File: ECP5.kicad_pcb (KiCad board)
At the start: 4 copper layers, 54.6 x 54.6 mm, 115 parts, among them J1 USB Type C, J2 EXT, Q1 MMST2222A, SW1 User, U1 LFE5U-85F-8BG381C, U2 IS25LP128F, U3 FT231XQ, U4 IS66WVE4M16EBLL-70BLI, U5 TLV62569DBVT, U6 TLV62569DBVT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

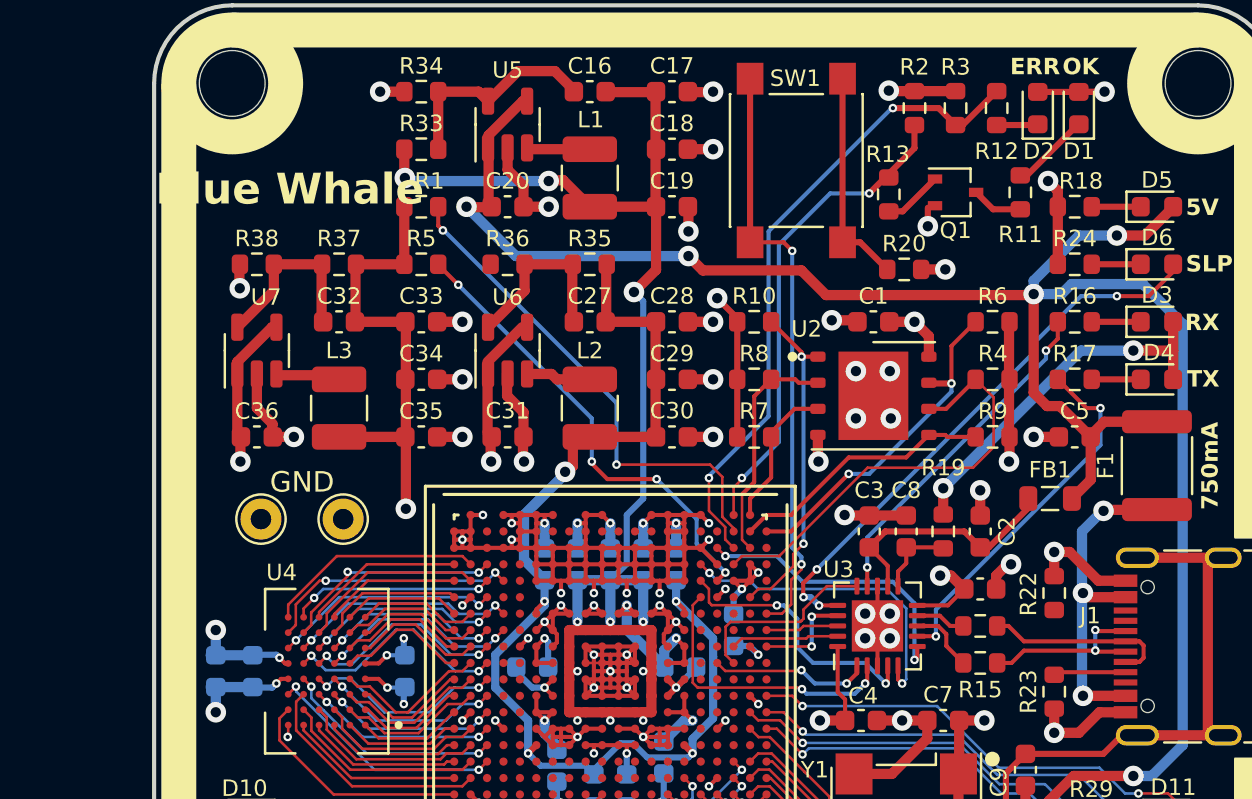
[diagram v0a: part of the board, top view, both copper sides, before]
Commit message: Switched to project library
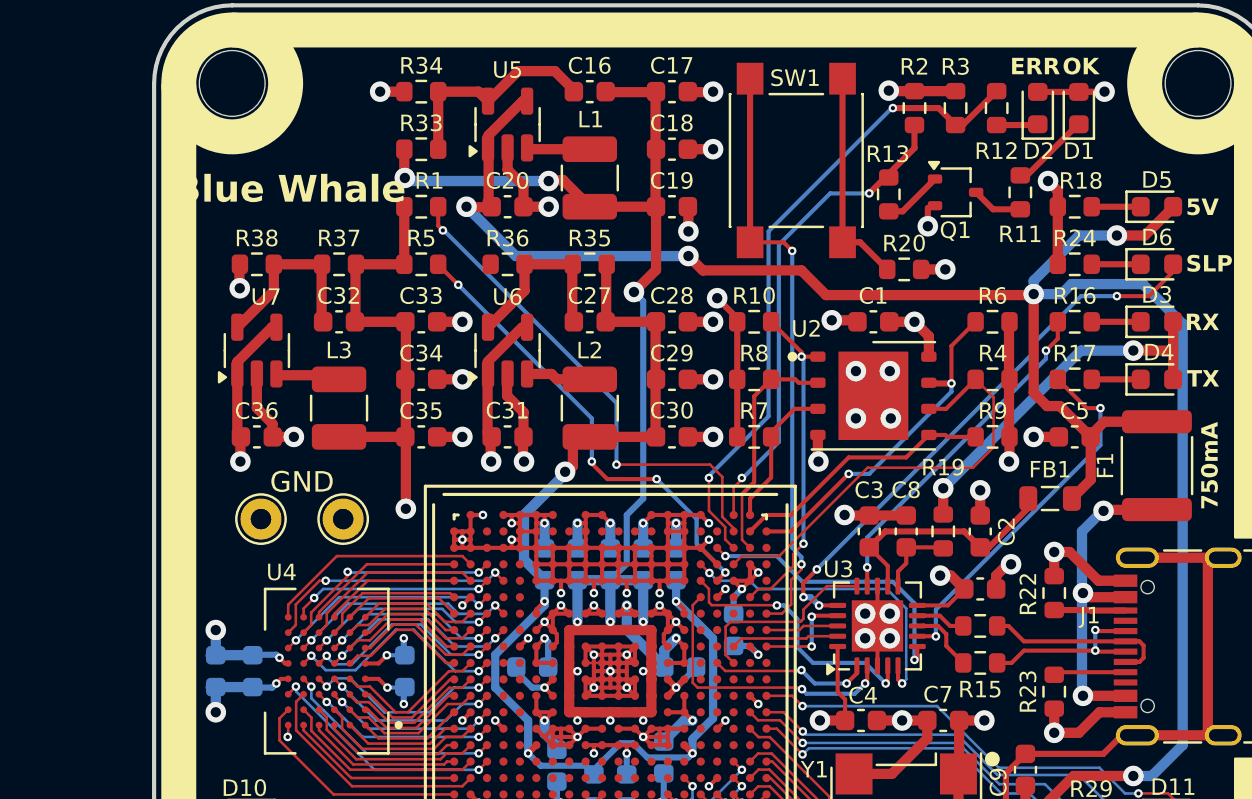
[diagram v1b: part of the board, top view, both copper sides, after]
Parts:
- F1: footprint Gil:Fuse_1812_4532Metric -> ECP5_RISCV:Fuse_1812_4532Metric
- J1: footprint Gil:USB_C_Receptacle_GCT_USB4105-xx-A_16P_TopMnt_Horizontal -> ECP5_RISCV:USB_C_Receptacle_GCT_USB4105-xx-A_16P_TopMnt_Horizontal
- J2: footprint Gil:FTS-120-02-L-DV -> ECP5_RISCV:FTS-120-02-L-DV
- U1: footprint Gil:BGA-381_pitch0.8mm_dia0.4mm -> ECP5_RISCV:BGA-381_pitch0.8mm_dia0.4mm
- U2: footprint Gil:WSON-8-1EP_6x5mm_P1.27mm_EP3.4x4.3mm -> ECP5_RISCV:WSON-8-1EP_6x5mm_P1.27mm_EP3.4x4.3mm
- U4: footprint Gil:BGA48C75P8X6_800X600X120N -> ECP5_RISCV:BGA48C75P8X6_800X600X120N
- Y1: footprint Gil:Oscillator_SMD_Diodes_FN-4Pin_7.0x5.0mm -> ECP5_RISCV:Oscillator_SMD_Diodes_FN-4Pin_7.0x5.0mm
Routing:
- net Net-(J1-CC2): track 0.00 -> 3.43 mm

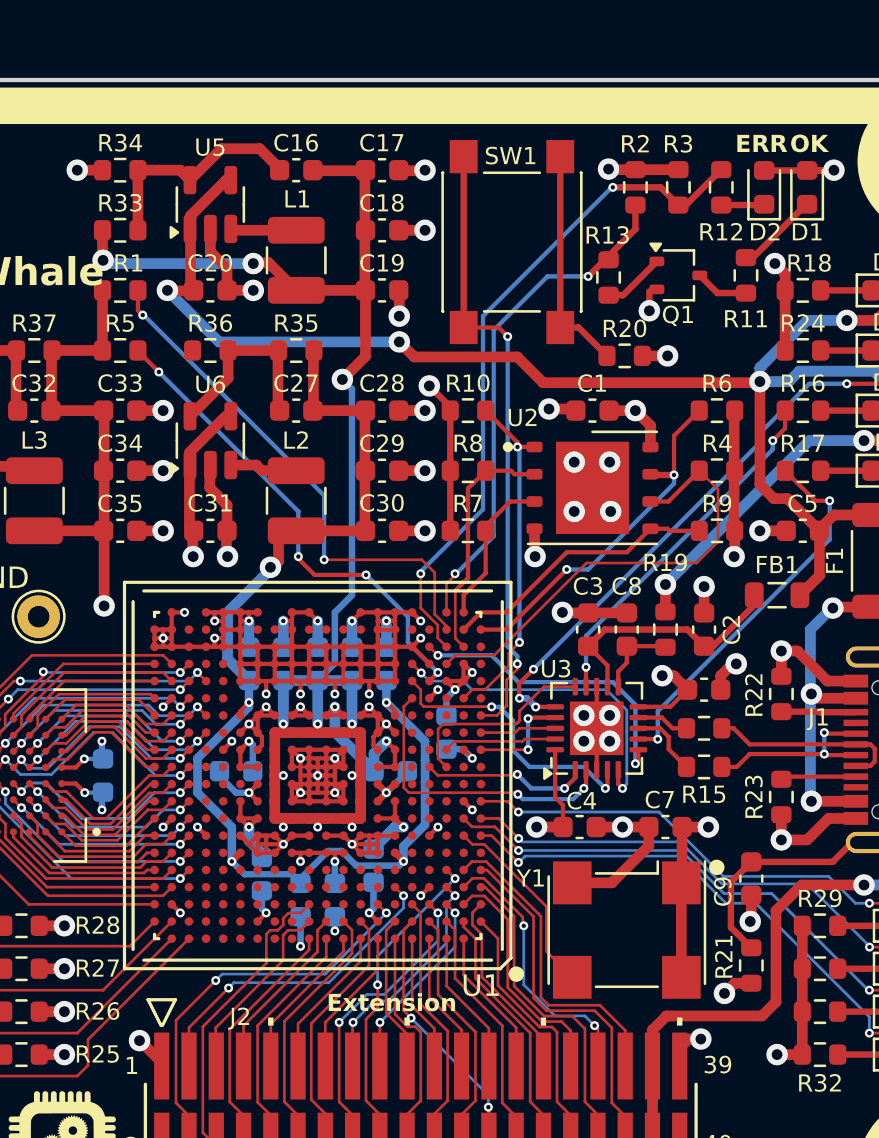
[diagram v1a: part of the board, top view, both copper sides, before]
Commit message: Changed the name of the project path to ECP5_BGA381_RISCV
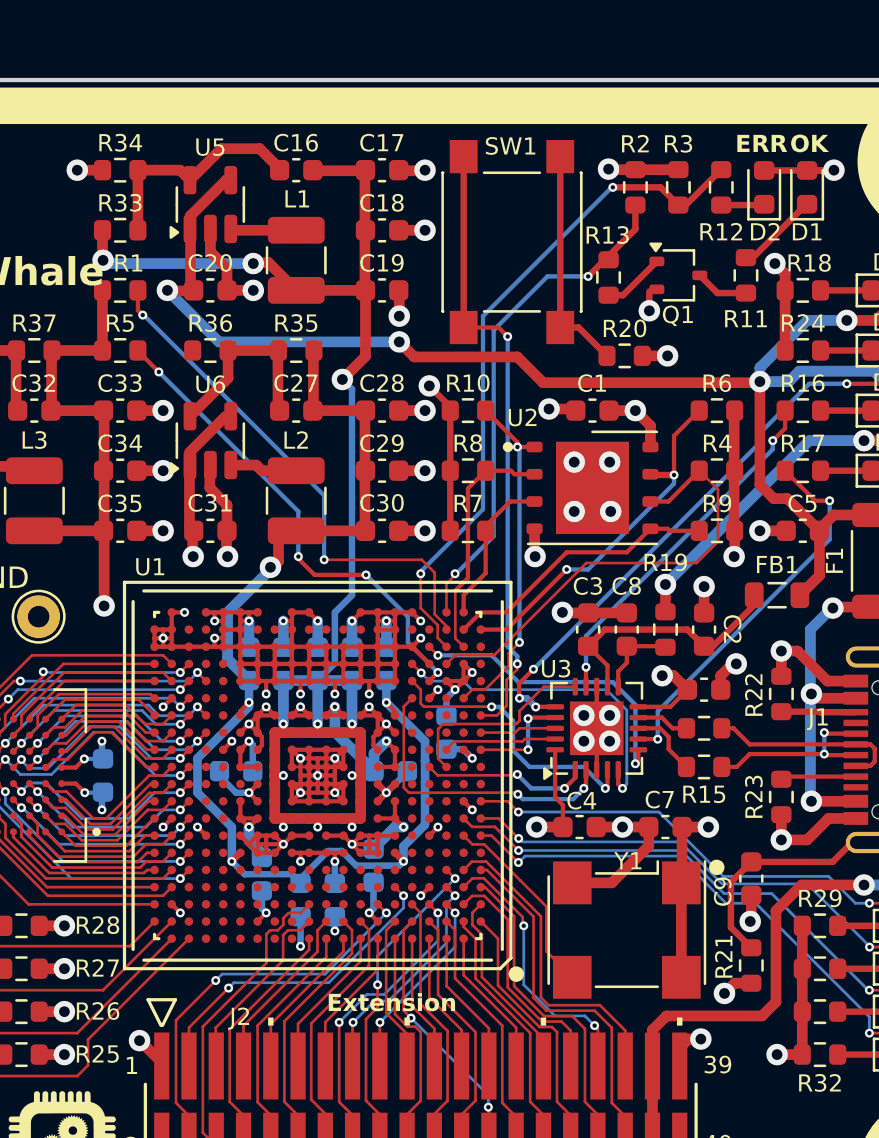
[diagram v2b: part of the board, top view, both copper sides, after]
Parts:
- F1: footprint ECP5_RISCV:Fuse_1812_4532Metric -> ECP5_BGA381_RISCV:Fuse_1812_4532Metric
- J1: footprint ECP5_RISCV:USB_C_Receptacle_GCT_USB4105-xx-A_16P_TopMnt_Horizontal -> ECP5_BGA381_RISCV:USB_C_Receptacle_GCT_USB4105-xx-A_16P_TopMnt_Horizontal
- J2: footprint ECP5_RISCV:FTS-120-02-L-DV -> ECP5_BGA381_RISCV:FTS-120-02-L-DV
- U1: footprint ECP5_RISCV:BGA-381_pitch0.8mm_dia0.4mm -> ECP5_BGA381_RISCV:BGA-381_pitch0.8mm_dia0.4mm
- U2: footprint ECP5_RISCV:WSON-8-1EP_6x5mm_P1.27mm_EP3.4x4.3mm -> ECP5_BGA381_RISCV:WSON-8-1EP_6x5mm_P1.27mm_EP3.4x4.3mm
- U4: footprint ECP5_RISCV:BGA48C75P8X6_800X600X120N -> ECP5_BGA381_RISCV:BGA48C75P8X6_800X600X120N
- Y1: footprint ECP5_RISCV:Oscillator_SMD_Diodes_FN-4Pin_7.0x5.0mm -> ECP5_BGA381_RISCV:Oscillator_SMD_Diodes_FN-4Pin_7.0x5.0mm
